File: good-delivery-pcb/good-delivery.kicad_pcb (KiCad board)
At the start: 2 copper layers, 190.5 x 76.2 mm, 99 parts, among them J2 SWD, J3 USB_C_Receptacle_USB2.0, SW1 RESET, SW2 BOOTSEL, U1 RP2040, U2 W25Q128JVS, U3 XC6206P332MR, Y1 12MHz

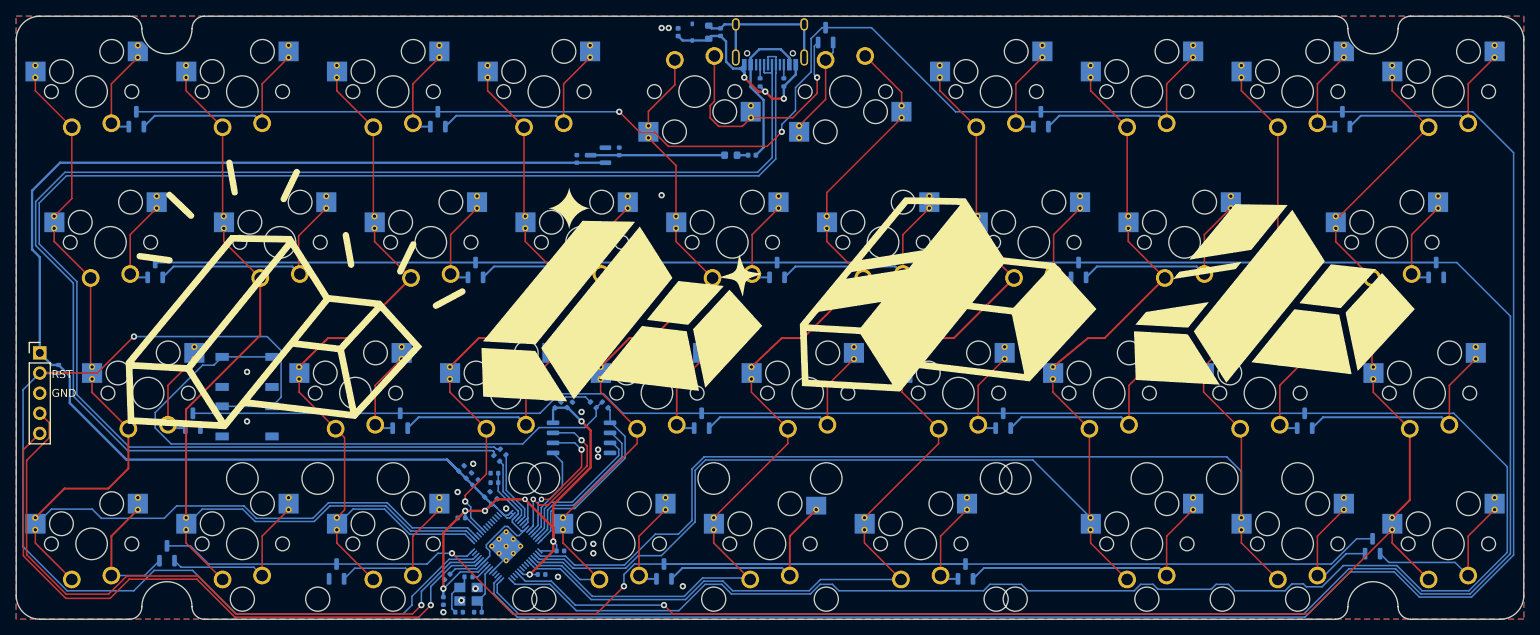
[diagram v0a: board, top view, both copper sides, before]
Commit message: Added option to solder MX corner switches for improved gummy o-ring support with 3-pin switches.
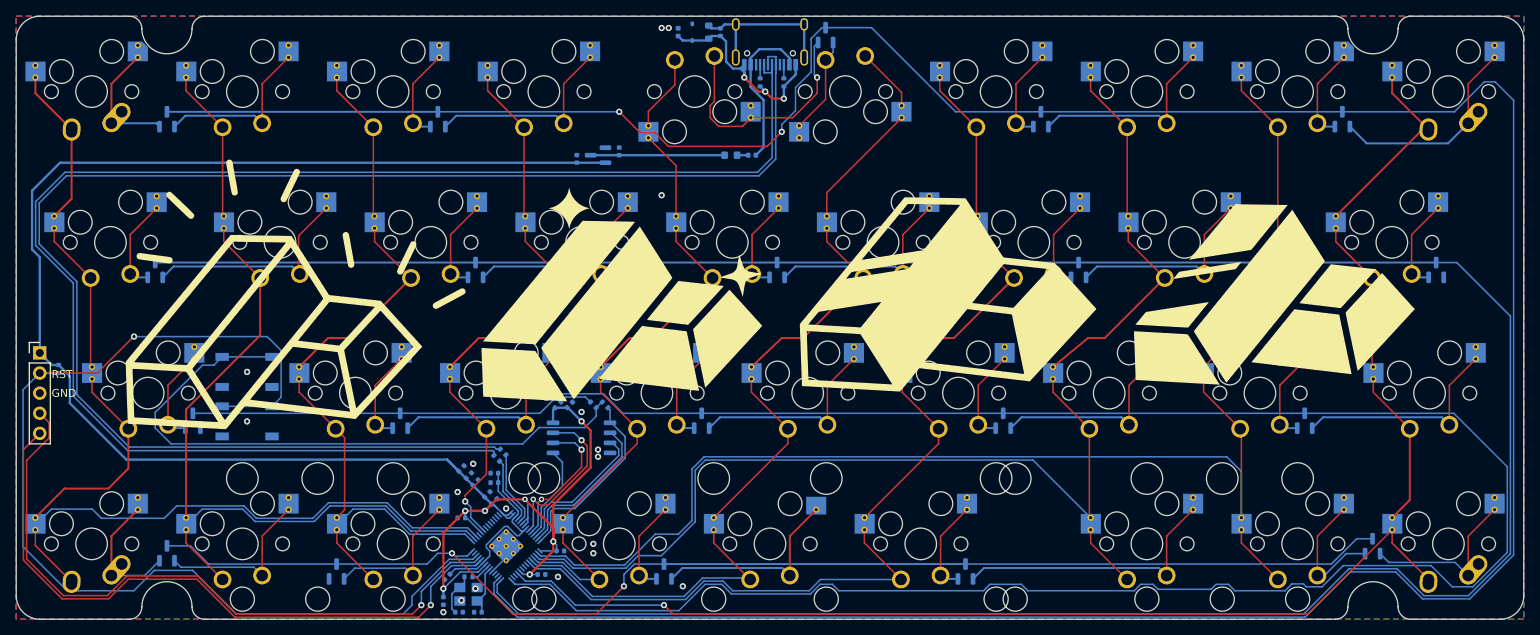
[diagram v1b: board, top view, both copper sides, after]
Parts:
- moved D1 3.87 mm to (66.7, 69.6)
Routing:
- net Net-(MX1-ROW): track 11.5 -> 16.0 mm
- net Net-(MX6-ROW): track 25.6 -> 21.7 mm
- net ROW 0: track 382.4 -> 385.8 mm
- net Net-(MX35-ROW): track 25.6 -> 26.6 mm
